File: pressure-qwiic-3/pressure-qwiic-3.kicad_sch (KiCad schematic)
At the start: 14 parts, among them IC1 SC18IS606PWJ, J1 Conn_01x04_Male, J2 Conn_01x04_Male, J3 Conn_01x04_Male, U1 TruStability_SPI, U2 TruStability_SPI, U3 TruStability_SPI

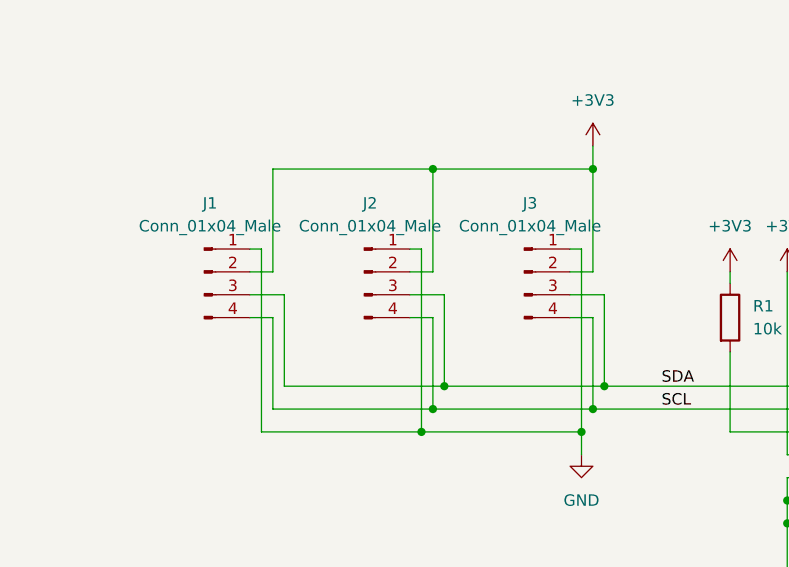
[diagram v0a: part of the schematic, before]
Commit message: Fixed QWIIC pinouts. Added QWIIC logo.
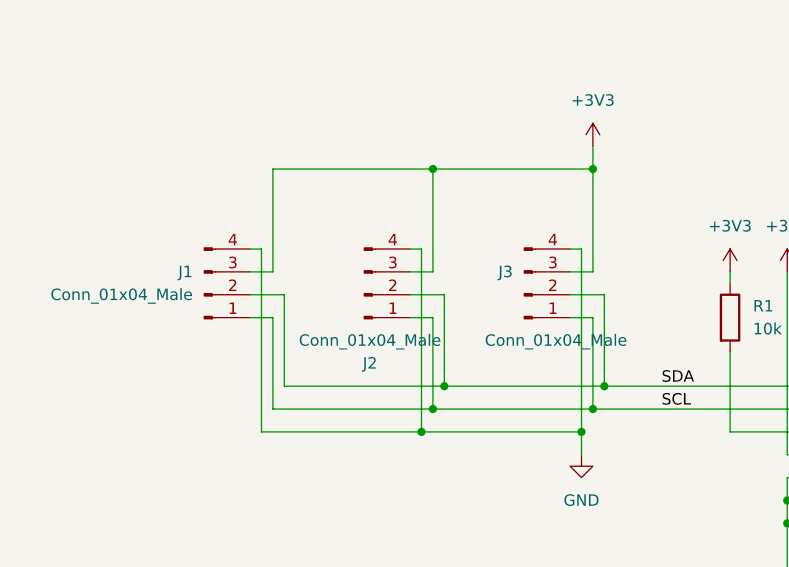
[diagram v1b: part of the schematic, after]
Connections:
- net +3V3: now also J1.3 (Pin_3), J2.3 (Pin_3), J3.3 (Pin_3); no longer J1.2 (Pin_2), J2.2 (Pin_2), J3.2 (Pin_2)
- net GND: now also J1.4 (Pin_4), J2.4 (Pin_4), J3.4 (Pin_4); no longer J1.1 (Pin_1), J2.1 (Pin_1), J3.1 (Pin_1)
- net SCL: now also J1.1 (Pin_1), J2.1 (Pin_1), J3.1 (Pin_1); no longer J1.4 (Pin_4), J2.4 (Pin_4), J3.4 (Pin_4)
- net SDA: now also J1.2 (Pin_2), J2.2 (Pin_2), J3.2 (Pin_2); no longer J1.3 (Pin_3), J2.3 (Pin_3), J3.3 (Pin_3)
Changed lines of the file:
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@@
     (pin "1")
   )
-  (symbol (lib_id "Connector:Conn_01x04_Male") (at 54.61 85.09 0) (unit 1)
-    (in_bom yes) (on_board yes) (fields_autoplaced)
-    (property "Reference" "J1" (id 0) (at 55.245 77.47 0))
-    (property "Value" "Conn_01x04_Male" (id 1) (at 55.245 80.01 0))
-    (property "Footprint" "airball-hardware:JST_SH_BM04B-SRSS-TB_1x04-1MP_P1.00mm_Vertical" (id 2) (at 54.61 85.09 0)
-      (effects (font (size 1.27 1.27)) hide)
-    )
-    (property "Datasheet" "~" (id 3) (at 54.61 85.09 0)
+  (symbol (lib_id "Connector:Conn_01x04_Male") (at 54.61 87.63 0) (mirror x) (unit 1)
+    (in_bom yes) (on_board yes) (fields_autoplaced)
+    (property "Reference" "J1" (id 0) (at 53.34 85.0899 0)
+      (effects (font (size 1.27 1.27)) (justify right))
+    )
+    (property "Value" "Conn_01x04_Male" (id 1) (at 53.34 87.6299 0)
+      (effects (font (size 1.27 1.27)) (justify right))
+    )
+    (property "Footprint" "airball-hardware:JST_SH_BM04B-SRSS-TB_1x04-1MP_P1.00mm_Vertical" (id 2) (at 54.61 87.63 0)
+      (effects (font (size 1.27 1.27)) hide)
+    )
+    (property "Datasheet" "~" (id 3) (at 54.61 87.63 0)
       (effects (font (size 1.27 1.27)) hide)
     )
@@
     (pin "9")
   )
-  (symbol (lib_id "Connector:Conn_01x04_Male") (at 72.39 85.09 0) (unit 1)
+  (symbol (lib_id "Connector:Conn_01x04_Male") (at 72.39 87.63 0) (mirror x) (unit 1)
     (in_bom yes) (on_board yes)
-    (property "Reference" "J2" (id 0) (at 73.025 77.47 0))
-    (property "Value" "Conn_01x04_Male" (id 1) (at 73.025 80.01 0))
-    (property "Footprint" "airball-hardware:JST_SH_BM04B-SRSS-TB_1x04-1MP_P1.00mm_Vertical" (id 2) (at 72.39 62.23 0)
-      (effects (font (size 1.27 1.27)) hide)
-    )
-    (property "Datasheet" "~" (id 3) (at 72.39 85.09 0)
-      (effects (font (size 1.27 1.27)) hide)
-    )
-    (pin "1")
-    (pin "2")
-    (pin "3")
-    (pin "4")
-  )
-  (symbol (lib_id "Connector:Conn_01x04_Male") (at 90.17 85.09 0) (unit 1)
-    (in_bom yes) (on_board yes) (fields_autoplaced)
-    (property "Reference" "J3" (id 0) (at 90.805 77.47 0))
-    (property "Value" "Conn_01x04_Male" (id 1) (at 90.805 80.01 0))
-    (property "Footprint" "airball-hardware:JST_SH_BM04B-SRSS-TB_1x04-1MP_P1.00mm_Vertical" (id 2) (at 90.17 85.09 0)
-      (effects (font (size 1.27 1.27)) hide)
-    )
-    (property "Datasheet" "~" (id 3) (at 90.17 85.09 0)
-      (effects (font (size 1.27 1.27)) hide)
-    )
+    (property "Reference" "J2" (id 0) (at 73.025 95.25 0))
+    (property "Value" "Conn_01x04_Male" (id 1) (at 73.025 92.71 0))
+    (property "Footprint" "airball-hardware:JST_SH_BM04B-SRSS-TB_1x04-1MP_P1.00mm_Vertical" (id 2) (at 72.39 110.49 0)
+      (effects (font (size 1.27 1.27)) hide)
+    )
+    (property "Datasheet" "~" (id 3) (at 72.39 87.63 0)
+      (effects (font (size 1.27 1.27)) hide)
+    )
+    (pin "1")
+    (pin "2")
+    (pin "3")
+    (pin "4")
+  )
+  (symbol (lib_id "Connector:Conn_01x04_Male") (at 90.17 87.63 0) (mirror x) (unit 1)
+    (in_bom yes) (on_board yes)
+    (property "Reference" "J3" (id 0) (at 88.9 85.0899 0)
+      (effects (font (size 1.27 1.27)) (justify right))
+    )
+    (property "Value" "Conn_01x04_Male" (id 1) (at 101.6 92.71 0)
+      (effects (font (size 1.27 1.27)) (justify right))
+    )
+    (property "Footprint" "airball-hardware:JST_SH_BM04B-SRSS-TB_1x04-1MP_P1.00mm_Vertical" (id 2) (at 90.17 87.63 0)
+      (effects (font (size 1.27 1.27)) hide)
+    )
+    (property "Datasheet" "~" (id 3) (at 90.17 87.63 0)
+      (effects (font (size 1.27 1.27)) hide)
+    )

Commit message: Almost complete.
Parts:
- added J4: Conn_01x04_Male, airball-hardware:JST_SH_BM04B-SRSS-TB_1x04-1MP_P1.00mm_Vertical, symbol Connector:Conn_01x04_Male
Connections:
- net +3V3: now also J4.3 (Pin_3)
- net GND: now also J4.4 (Pin_4)
- net SCL: now also J4.1 (Pin_1)
- net SDA: now also J4.2 (Pin_2)
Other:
- moved on the sheet: J1, J2, J3

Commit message: More changes. Should be ready now.
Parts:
- added C1: 0.1uF, Capacitor_SMD:C_0603_1608Metric, symbol Device:C
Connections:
- net +3V3: now also C1.1
- net GND: now also C1.2
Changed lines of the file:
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@@
   (junction (at 119.38 113.03) (diameter 0) (color 0 0 0 0)
   )
+  (junction (at 166.37 107.95) (diameter 0) (color 0 0 0 0)
+  )
   (junction (at 213.36 73.66) (diameter 0) (color 0 0 0 0)
   )
   (junction (at 179.07 76.2) (diameter 0) (color 0 0 0 0)
   )
+  (junction (at 180.34 129.54) (diameter 0) (color 0 0 0 0)
+  )
   (junction (at 59.69 97.79) (diameter 0) (color 0 0 0 0)
   )
@@
     (stroke (width 0) (type default) (color 0 0 0 0))
   )
+  (wire (pts (xy 166.37 100.33) (xy 166.37 107.95))
+    (stroke (width 0) (type default) (color 0 0 0 0))
+  )
   (wire (pts (xy 73.66 82.55) (xy 74.93 82.55))
     (stroke (width 0) (type default) (color 0 0 0 0))
@@
     (stroke (width 0) (type default) (color 0 0 0 0))
   )
+  (wire (pts (xy 166.37 129.54) (xy 180.34 129.54))
+    (stroke (width 0) (type default) (color 0 0 0 0))
+  )
   (wire (pts (xy 99.06 87.63) (xy 99.06 97.79))
     (stroke (width 0) (type default) (color 0 0 0 0))
@@
     (stroke (width 0) (type default) (color 0 0 0 0))
   )
+  (wire (pts (xy 166.37 107.95) (xy 166.37 121.92))
+    (stroke (width 0) (type default) (color 0 0 0 0))
+  )
   (wire (pts (xy 120.65 120.65) (xy 214.63 120.65))
     (stroke (width 0) (type default) (color 0 0 0 0))
@@
     (stroke (width 0) (type default) (color 0 0 0 0))
   )
-  (wire (pts (xy 168.91 105.41) (xy 168.91 124.46))
+  (wire (pts (xy 180.34 105.41) (xy 180.34 129.54))
     (stroke (width 0) (type default) (color 0 0 0 0))
   )
@@
     (stroke (width 0) (type default) (color 0 0 0 0))
   )
+  (wire (pts (xy 180.34 129.54) (xy 180.34 132.08))
+    (stroke (width 0) (type default) (color 0 0 0 0))
+  )
   (wire (pts (xy 214.63 120.65) (xy 214.63 76.2))
     (stroke (width 0) (type default) (color 0 0 0 0))
@@
     (stroke (width 0) (type default) (color 0 0 0 0))
   )
-  (wire (pts (xy 166.37 100.33) (xy 166.37 107.95))
-    (stroke (width 0) (type default) (color 0 0 0 0))
-  )
   (wire (pts (xy 74.93 82.55) (xy 74.93 102.87))
     (stroke (width 0) (type default) (color 0 0 0 0))
@@
     (stroke (width 0) (type default) (color 0 0 0 0))
   )
-  (wire (pts (xy 165.1 105.41) (xy 168.91 105.41))
+  (wire (pts (xy 165.1 105.41) (xy 180.34 105.41))
     (stroke (width 0) (type default) (color 0 0 0 0))
   )
@@
     (stroke (width 0) (type default) (color 0 0 0 0))
   )
-  (label "SCLK" (at 175.26 110.49 0)
+  (label "SCLK" (at 195.58 110.49 0)
     (effects (font (size 1.27 1.27)) (justify left bottom))
   )
-  (label "MISO" (at 175.26 102.87 0)
+  (label "MISO" (at 195.58 102.87 0)
     (effects (font (size 1.27 1.27)) (justify left bottom))
   )
-  (label "!CS1" (at 175.26 97.79 0)
+  (label "!CS1" (at 195.58 97.79 0)
     (effects (font (size 1.27 1.27)) (justify left bottom))
   )
@@
     (effects (font (size 1.27 1.27)) (justify left bottom))
   )
-  (label "!CS0" (at 175.26 115.57 0)
+  (label "!CS0" (at 195.58 115.57 0)
     (effects (font (size 1.27 1.27)) (justify left bottom))
   )
@@
     (effects (font (size 1.27 1.27)) (justify left bottom))
   )
-  (label "!CS2" (at 175.26 120.65 0)
+  (label "!CS2" (at 195.58 120.65 0)
     (effects (font (size 1.27 1.27)) (justify left bottom))
   )
@@
     (pin "2")
   )
-  (symbol (lib_id "power:GND") (at 168.91 124.46 0) (unit 1)
-    (in_bom yes) (on_board yes) (fields_autoplaced)
-    (property "Reference" "#PWR07" (id 0) (at 168.91 130.81 0)
-      (effects (font (size 1.27 1.27)) hide)
-    )
-    (property "Value" "GND" (id 1) (at 168.91 129.54 0))
-    (property "Footprint" "" (id 2) (at 168.91 124.46 0)
-      (effects (font (size 1.27 1.27)) hide)
-    )
-    (property "Datasheet" "" (id 3) (at 168.91 124.46 0)
+  (symbol (lib_id "power:GND") (at 180.34 132.08 0) (unit 1)
+    (in_bom yes) (on_board yes) (fields_autoplaced)
+    (property "Reference" "#PWR07" (id 0) (at 180.34 138.43 0)
+      (effects (font (size 1.27 1.27)) hide)
+    )
+    (property "Value" "GND" (id 1) (at 180.34 137.16 0))
+    (property "Footprint" "" (id 2) (at 180.34 132.08 0)
+      (effects (font (size 1.27 1.27)) hide)
+    )
+    (property "Datasheet" "" (id 3) (at 180.34 132.08 0)
       (effects (font (size 1.27 1.27)) hide)
     )
@@
     )
     (property "Datasheet" "~" (id 3) (at 113.03 90.17 0)
+      (effects (font (size 1.27 1.27)) hide)
+    )
+    (pin "1")
+    (pin "2")
+  )
+  (symbol (lib_id "Device:C") (at 166.37 125.73 0) (unit 1)
+    (in_bom yes) (on_board yes)
+    (property "Reference" "C1" (id 0) (at 170.18 124.4599 0)
+      (effects (font (size 1.27 1.27)) (justify left))
+    )
+    (property "Value" "0.1uF" (id 1) (at 170.18 126.9999 0)
+      (effects (font (size 1.27 1.27)) (justify left))
+    )
+    (property "Footprint" "Capacitor_SMD:C_0603_1608Metric" (id 2) (at 167.3352 129.54 0)
+      (effects (font (size 1.27 1.27)) hide)
+    )
+    (property "Datasheet" "~" (id 3) (at 166.37 125.73 0)
       (effects (font (size 1.27 1.27)) hide)
     )
@@
       (reference "#PWR010") (unit 1) (value "GND") (footprint "")
     )
+    (path "/d9c14104-fac3-4991-8f38-0c260a11ad9d"
+      (reference "C1") (unit 1) (value "0.1uF") (footprint "Capacitor_SMD:C_0603_1608Metric")
+    )
     (path "/66e8dd5d-d4c9-45a2-b7c9-52c0db743ba6"

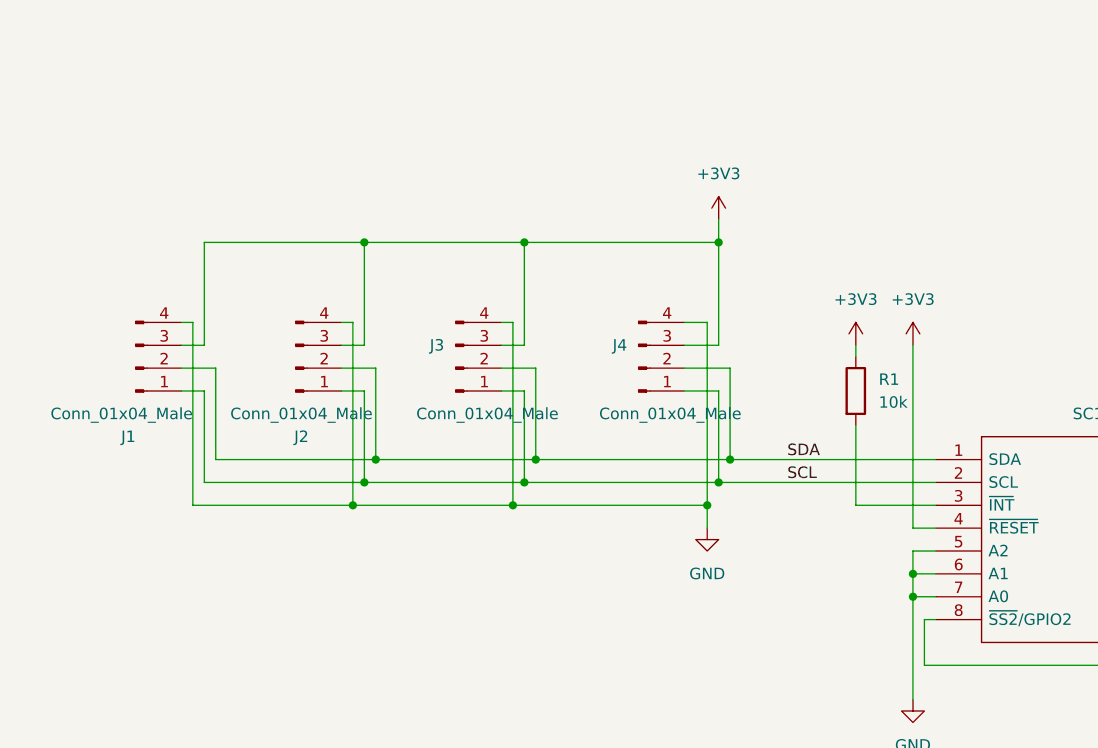
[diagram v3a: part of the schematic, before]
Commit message: Moved to 4 layer PCB and shrank the size. Re-routed.
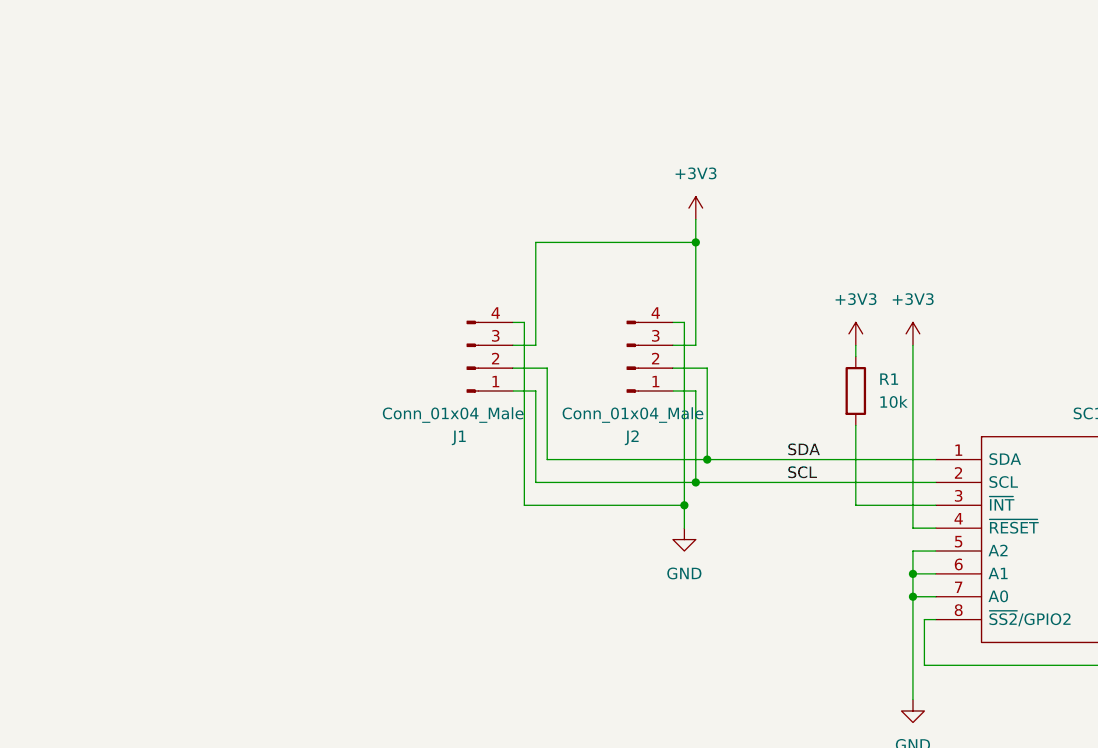
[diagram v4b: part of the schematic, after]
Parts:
- removed J3, J4: Conn_01x04_Male, airball-hardware:JST_SH_BM04B-SRSS-TB_1x04-1MP_P1.00mm_Vertical, symbol Connector:Conn_01x04_Male
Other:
- moved on the sheet: J1, J2
